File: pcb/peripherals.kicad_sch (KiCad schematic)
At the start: 12 parts, among them J10 BM08B-SRSS-TB, J14 BM03B-SRSS-TB, J3 BM03B-SRSS-TB, J8 BM04B-SRSS-TB, J9 BM04B-SRSS-TB, Q1 MMBT2222A

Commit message: Fixed footprint for Buzzer, XFC, USB ESD, and Power Switcher
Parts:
- LS1: footprint CRG Makes:CMT050275SMTTR -> CRG Makes:FUET-5025
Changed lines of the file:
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@@
 			)
 		)
-		(property "Footprint" "CRG Makes:CMT050275SMTTR"
+		(property "Footprint" "CRG Makes:FUET-5025"
 			(at 232.41 125.4 0)
 			(effects

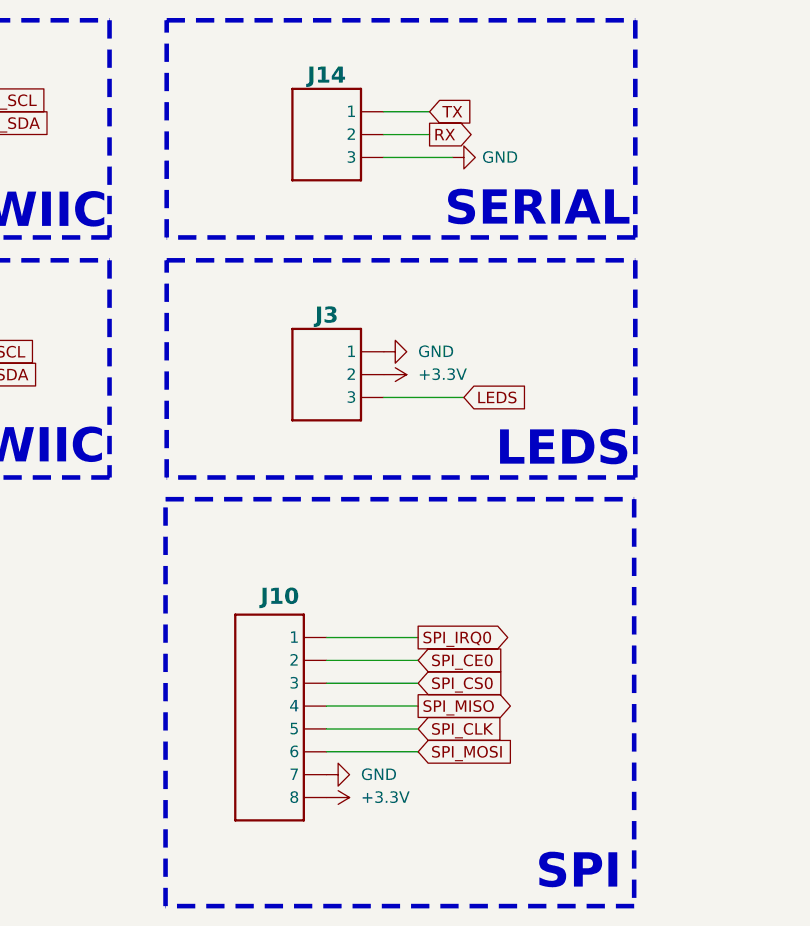
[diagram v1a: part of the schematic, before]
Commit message: Added test points. Fixed license file.
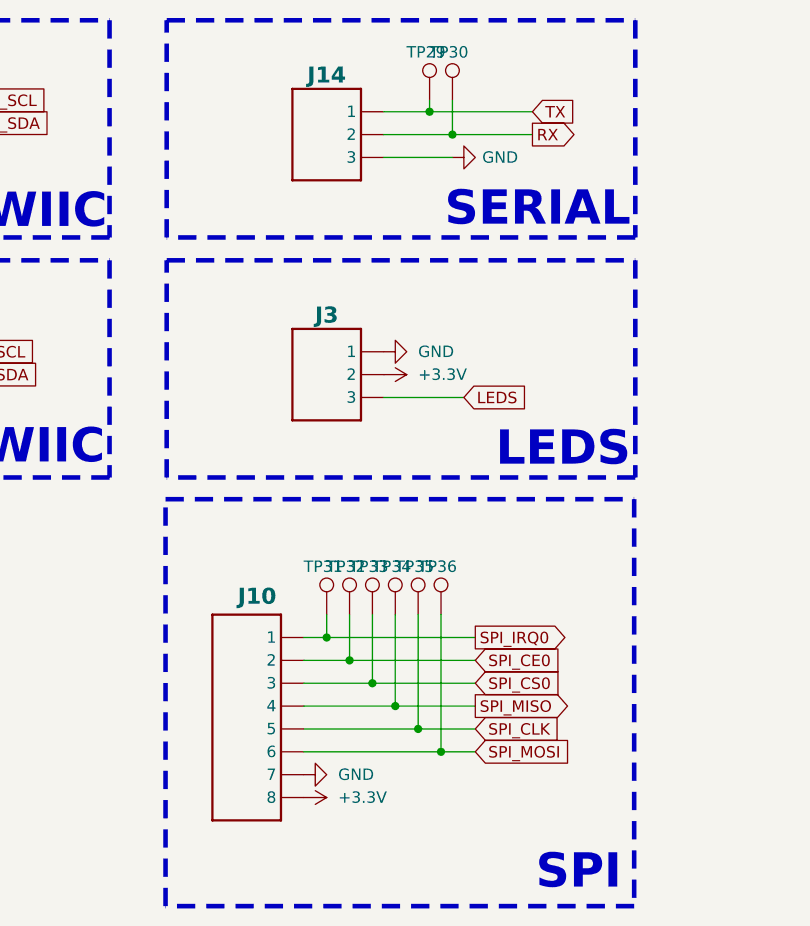
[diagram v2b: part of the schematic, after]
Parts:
- added TP29, TP30, TP31, TP32, TP33, TP34, TP35, TP36: TP, CRGM Mechanical:TestPoint_Pad_D1.0mm, symbol Connector:TestPoint
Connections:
- net RX: now also TP30.1
- net SPI_CE0: now also TP32.1
- net SPI_CLK: now also TP35.1
- net SPI_CS0: now also TP33.1
- net SPI_IRQ0: now also TP31.1
- net SPI_MISO: now also TP34.1
- net SPI_MOSI: now also TP36.1
- net TX: now also TP29.1
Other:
- moved on the sheet: J10

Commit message: Change name in schematic
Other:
- title: Node Hardware -> Hub Hardware
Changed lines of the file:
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@@
 	(paper "A4")
 	(title_block
-		(title "Node Hardware")
+		(title "Hub Hardware")
 		(date "<<release-date>>")
 		(rev "<<tag>>")

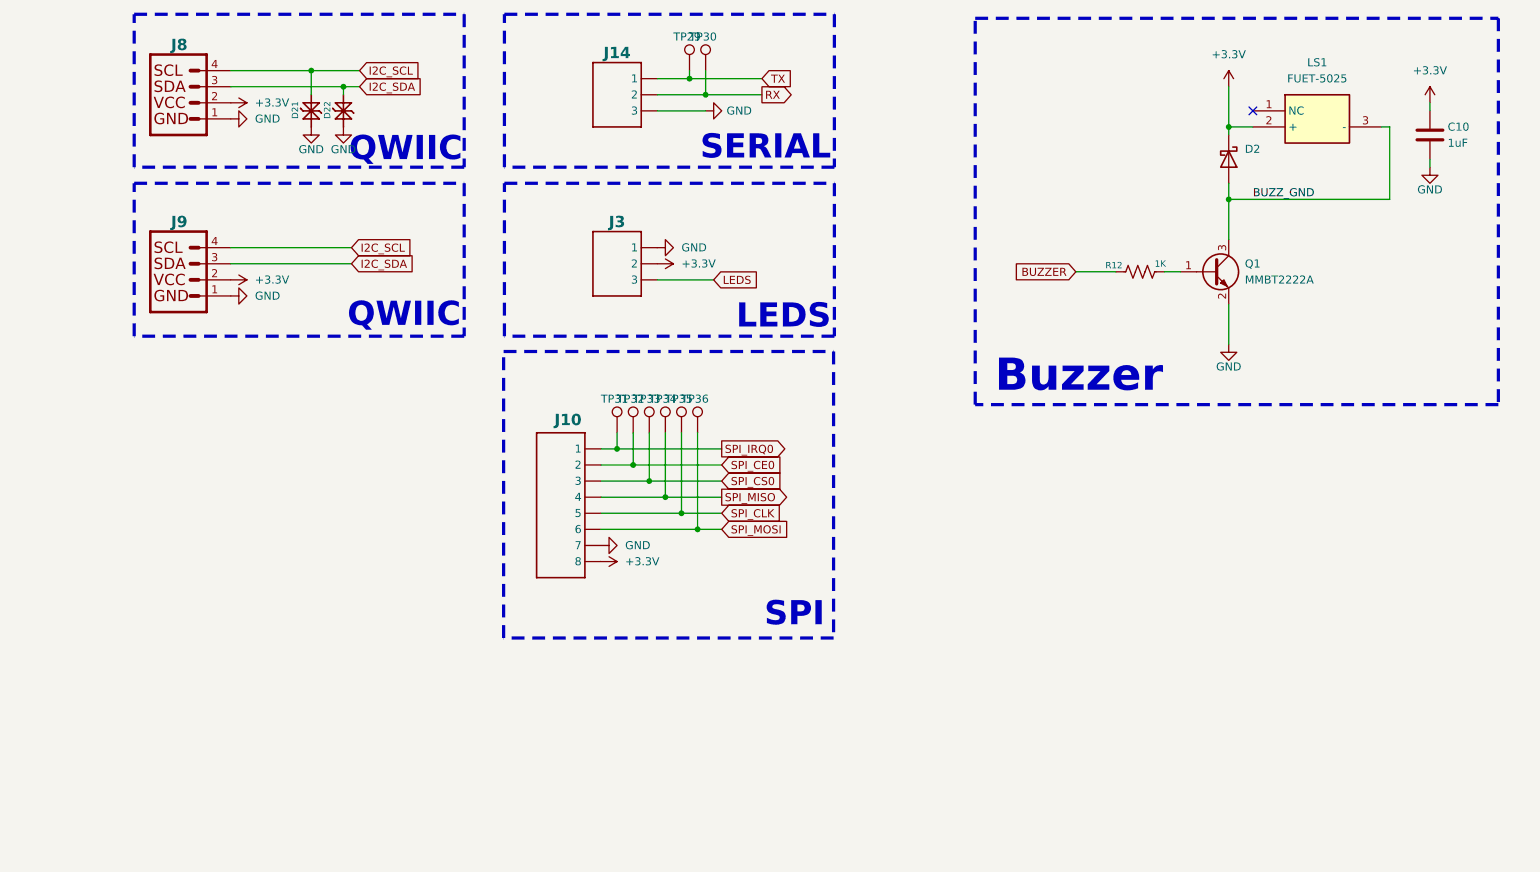
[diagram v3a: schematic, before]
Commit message: renamed pio to peripheral
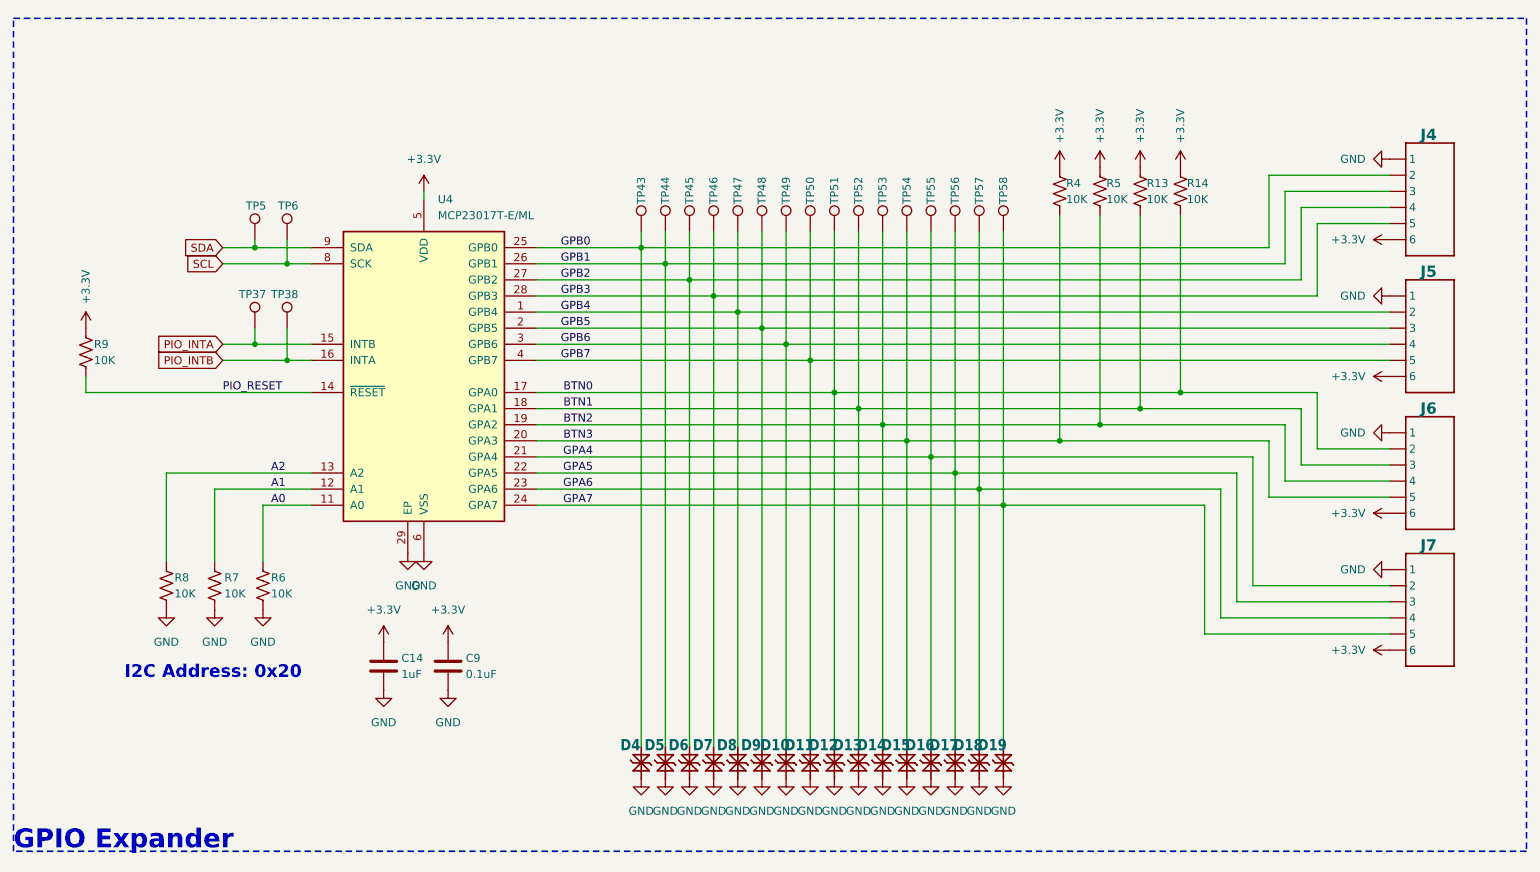
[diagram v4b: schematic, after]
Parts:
- removed C10: 1uF, Capacitor_SMD:C_0603_1608Metric, symbol Device:C
- removed D2: D_Schottky, Diode_SMD:D_SOD-523, symbol Device:D_Schottky
- removed D21, D22: PESD3V3S1BL, CRGM Passive:DFN1006-2, symbol CRGM Passive:PESD3V3S1BL
- removed J10: BM08B-SRSS-TB, CRGM Connector:JST_SH_BM08B-SRSS-TB_1x08-1MP_P1.00mm_Vertical, symbol CRGM Connector:JST-SH-8
- removed J14, J3: BM03B-SRSS-TB, CRGM Connector:JST_SH_BM03B-SRSS-TB_1x03-1MP_P1.00mm_Vertical, symbol CRGM Connector:JST-SH-3
- removed J8, J9: BM04B-SRSS-TB, CRGM Connector:JST_SH_BM04B-SRSS-TB_1x04-1MP_P1.00mm_Vertical, symbol CRGM Connector:QWIIC
- removed LS1: FUET-5025, CRG Makes:FUET-5025, symbol CRG Makes:CMT-0502-75-SMT-TR
- removed Q1: MMBT2222A, Package_TO_SOT_SMD:SOT-523, symbol Transistor_BJT:MMBT2222A
- removed R12: 1K, Resistor_SMD:R_0603_1608Metric, symbol Device:R_US
- removed TP29, TP30, TP31, TP32, TP33, TP34, TP35, TP36: TP, CRGM Mechanical:TestPoint_Pad_D1.0mm, symbol Connector:TestPoint
- added C14: 1uF, CRGM Passive:C_0603_1608Metric, symbol Device:C
- added C9: 0.1uF, CRGM Passive:C_0603_1608Metric, symbol Device:C
- added D10, D11, D12, D13, D14, D15, D16, D17, D18, D19, D4, D5, D6, D7, D8, D9: PESD3V3S1BL, CRGM Passive:DFN1006-2, symbol CRGM Passive:PESD3V3S1BL
- added J4, J5, J6, J7: SM06B-SRSS-TB, CRGM Connector:JST_SH_SM06B-SRSS-TB_1x06-1MP_P1.00mm_Horizontal, symbol CRGM Connector:JST-SH-6
- added R13, R14, R4, R5, R6, R7, R8, R9: 10K, CRGM Passive:R_0603_1608Metric, symbol Device:R_US
- added TP37, TP38, TP43, TP44, TP45, TP46, TP47, TP48, TP49, TP5, TP50, TP51, TP52, TP53, TP54, TP55, TP56, TP57, TP58, TP6: ~, CRGM Mechanical:TestPoint_Pad_D1.0mm, symbol Connector:TestPoint
- added U4: MCP23017T-E/ML, CRG Makes:QFN-28-1EP_6x6mm_P0.65mm_EP4.25x4.25mm, symbol Interface_Expansion:MCP23017_ML
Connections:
- net +3.3V: now also C14.1, C9.1, J4.6, J5.6, J6.6, J7.6, R13.1, R14.1, R4.1, R5.1, R9.1, U4.5 (VDD)
- net GND: now also C14.2, C9.2, D10.1 (K1), D11.1 (K1), D12.1 (K1), D13.1 (K1), D14.1 (K1), D15.1 (K1), D16.1 (K1), D17.1 (K1), D18.1 (K1), D19.1 (K1), D4.1 (K1), D5.1 (K1), D6.1 (K1), D7.1 (K1), D8.1 (K1), D9.1 (K1), J4.1, J5.1, J6.1, J7.1, R6.2, R7.2, R8.2, U4.29 (EP), U4.6 (VSS)
- new net A0: R6.1, U4.11 (A0)
- new net A1: R7.1, U4.12 (A1)
- new net A2: R8.1, U4.13 (A2)
- new net BTN0: D12.2 (K2), J6.2, R14.2, TP51.1, U4.17 (GPA0)
- new net BTN1: D13.2 (K2), J6.3, R13.2, TP52.1, U4.18 (GPA1)
- new net BTN2: D14.2 (K2), J6.4, R5.2, TP53.1, U4.19 (GPA2)
- new net BTN3: D15.2 (K2), J6.5, R4.2, TP54.1, U4.20 (GPA3)
- new net GPA4: D16.2 (K2), J7.2, TP55.1, U4.21 (GPA4)
- new net GPA5: D17.2 (K2), J7.3, TP56.1, U4.22 (GPA5)
- new net GPA6: D18.2 (K2), J7.4, TP57.1, U4.23 (GPA6)
- new net GPA7: D19.2 (K2), J7.5, TP58.1, U4.24 (GPA7)
- new net GPB0: D4.2 (K2), J4.2, TP43.1, U4.25 (GPB0)
- new net GPB1: D5.2 (K2), J4.3, TP44.1, U4.26 (GPB1)
- new net GPB2: D6.2 (K2), J4.4, TP45.1, U4.27 (GPB2)
- new net GPB3: D7.2 (K2), J4.5, TP46.1, U4.28 (GPB3)
- new net GPB4: D8.2 (K2), J5.2, TP47.1, U4.1 (GPB4)
- new net GPB5: D9.2 (K2), J5.3, TP48.1, U4.2 (GPB5)
- new net GPB6: D10.2 (K2), J5.4, TP49.1, U4.3 (GPB6)
- new net GPB7: D11.2 (K2), J5.5, TP50.1, U4.4 (GPB7)
- new net PIO_INTA: TP37.1, U4.15 (INTB)
- new net PIO_INTB: TP38.1, U4.16 (INTA)
- new net PIO_RESET: R9.2, U4.14 (~{RESET})
- new net SCL: TP6.1, U4.8 (SCK)
- new net SDA: TP5.1, U4.9 (SDA)
- no-connect marks 1 -> 0
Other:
- note added: "GPIO Expander"
- note added: "I2C Address: 0x20"
- note removed: "Buzzer"
- note removed: "LEDS"
- note removed: "QWIIC"
- note removed: "SERIAL"
- note removed: "SPI"
- title: Hub Hardware -> Aquarius Hub

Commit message: Moved to vertical connectors
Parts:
- J4, J5, J6, J7: value SM06B-SRSS-TB -> BM06B-SRSS-TB; footprint CRGM Connector:JST_SH_SM06B-SRSS-TB_1x06-1MP_P1.00mm_Horizontal -> CRGM Connector:JST_SH_BM06B-SRSS-TB_1x06-1MP_P1.00mm_Vertical; Digikey 455-SM06B-SRSS-TBTR-ND -> 455-BM06B-SRSS-TBTR-ND; LCSC C2763616 -> C2904988; MPN SM06B-SRSS-TBT(LF)(SN) -> BM06B-SRSS-TBT(LF)(SN); Mouser 306-SM06BSRSSTBTLFSN -> 306-BM06BSRSSTBTLFSN
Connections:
- net +3.3V: now also J4.1, J5.1, J6.1, J7.1; no longer J4.6, J5.6, J6.6, J7.6
- net BTN0: now also J6.5; no longer J6.2
- net BTN1: now also J6.4; no longer J6.3
- net BTN2: now also J6.3; no longer J6.4
- net BTN3: now also J6.2; no longer J6.5
- net GND: now also J4.6, J5.6, J6.6, J7.6; no longer J4.1, J5.1, J6.1, J7.1
- net GPA4: now also J7.5; no longer J7.2
- net GPA5: now also J7.4; no longer J7.3
- net GPA6: now also J7.3; no longer J7.4
- net GPA7: now also J7.2; no longer J7.5
- net GPB0: now also J4.5; no longer J4.2
- net GPB1: now also J4.4; no longer J4.3
- net GPB2: now also J4.3; no longer J4.4
- net GPB3: now also J4.2; no longer J4.5
- net GPB4: now also J5.5; no longer J5.2
- net GPB5: now also J5.4; no longer J5.3
- net GPB6: now also J5.3; no longer J5.4
- net GPB7: now also J5.2; no longer J5.5

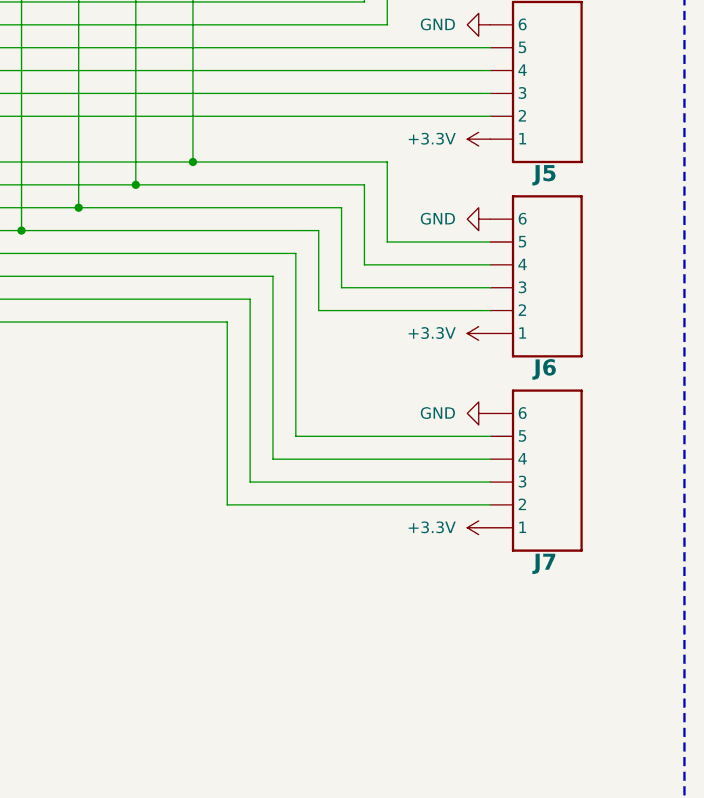
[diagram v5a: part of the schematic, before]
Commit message: Changed button connector to ground every other
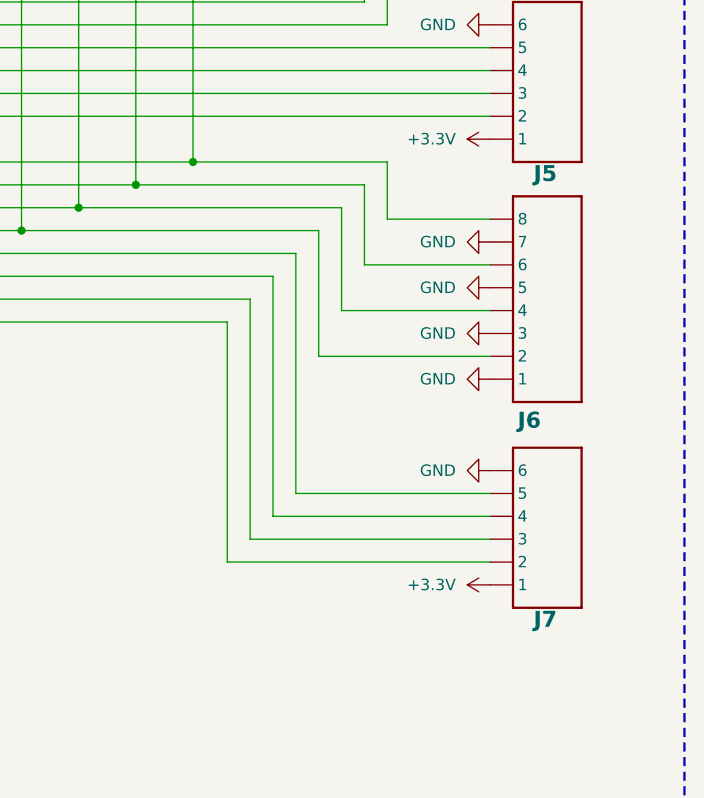
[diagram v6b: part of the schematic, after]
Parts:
- removed J6: BM06B-SRSS-TB, CRGM Connector:JST_SH_BM06B-SRSS-TB_1x06-1MP_P1.00mm_Vertical, symbol CRGM Connector:JST-SH-6
- added J6: BM08B-SRSS-TB, CRGM Connector:JST_SH_BM08B-SRSS-TB_1x08-1MP_P1.00mm_Vertical, symbol CRGM Connector:JST-SH-8
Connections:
- net BTN0: now also J6.8
- net BTN1: now also J6.6
- net BTN2: now also J6.4
- net BTN3: now also J6.2
- net GND: now also J6.1, J6.3, J6.5, J6.7
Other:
- moved on the sheet: J7

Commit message: Minor silkscreen changes.
Updated 2222 footprint
Ready for next release
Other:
- title: Aquarius Hub -> Aquarius Node
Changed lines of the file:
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@@
 	(paper "A4")
 	(title_block
-		(title "Aquarius Hub")
+		(title "Aquarius Node")
 		(date "<<release-date>>")
 		(rev "<<tag>>")

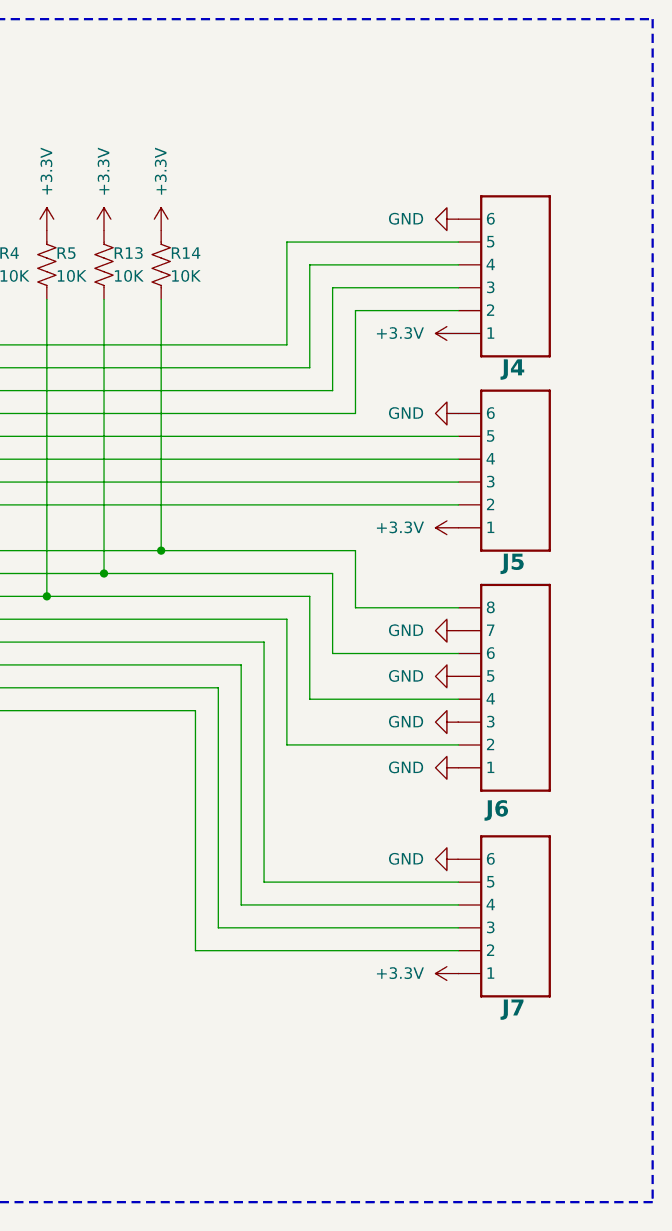
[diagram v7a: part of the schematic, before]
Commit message: Fixed part placement and missing model
Both display and 3.3 regulator were in the wrong place after updating from library!
LED was missing model
Minor silkscreen changes
Updated renders
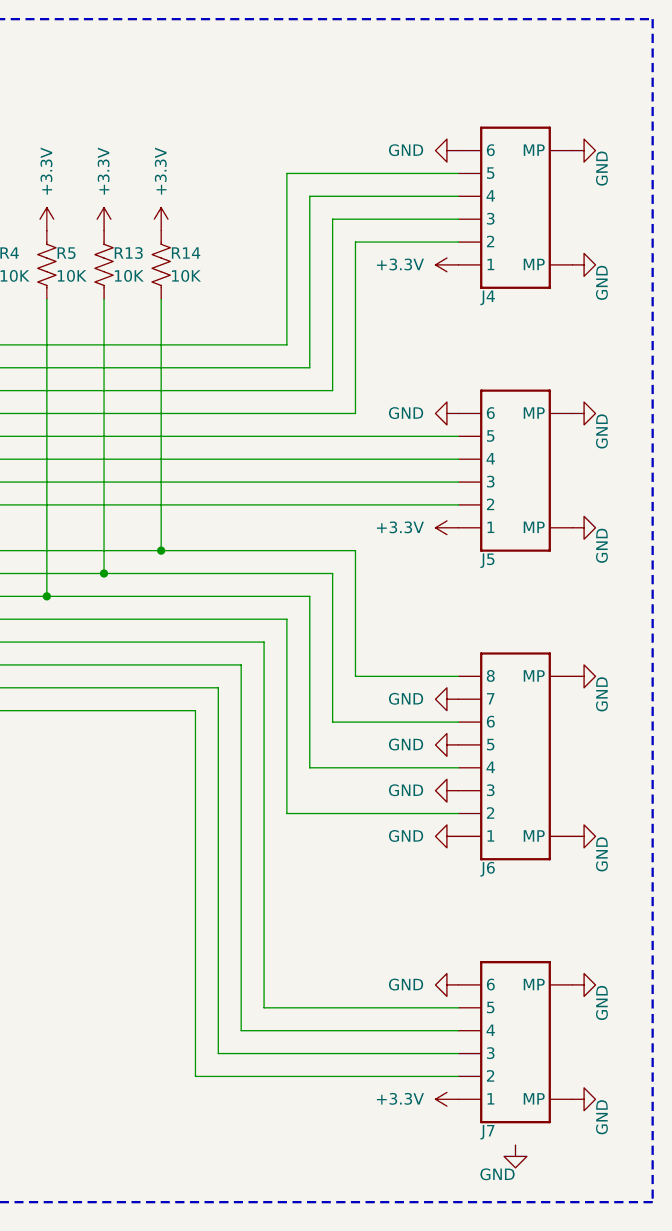
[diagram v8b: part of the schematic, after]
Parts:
- J4, J5, J7: value BM06B-SRSS-TB -> ~; LCSC C2904988 -> C2845374
- J6: value BM08B-SRSS-TB -> ~
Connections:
- net GND: now also J4.MP, J5.MP, J6.MP, J7.MP
